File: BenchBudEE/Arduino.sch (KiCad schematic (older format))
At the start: 14 parts

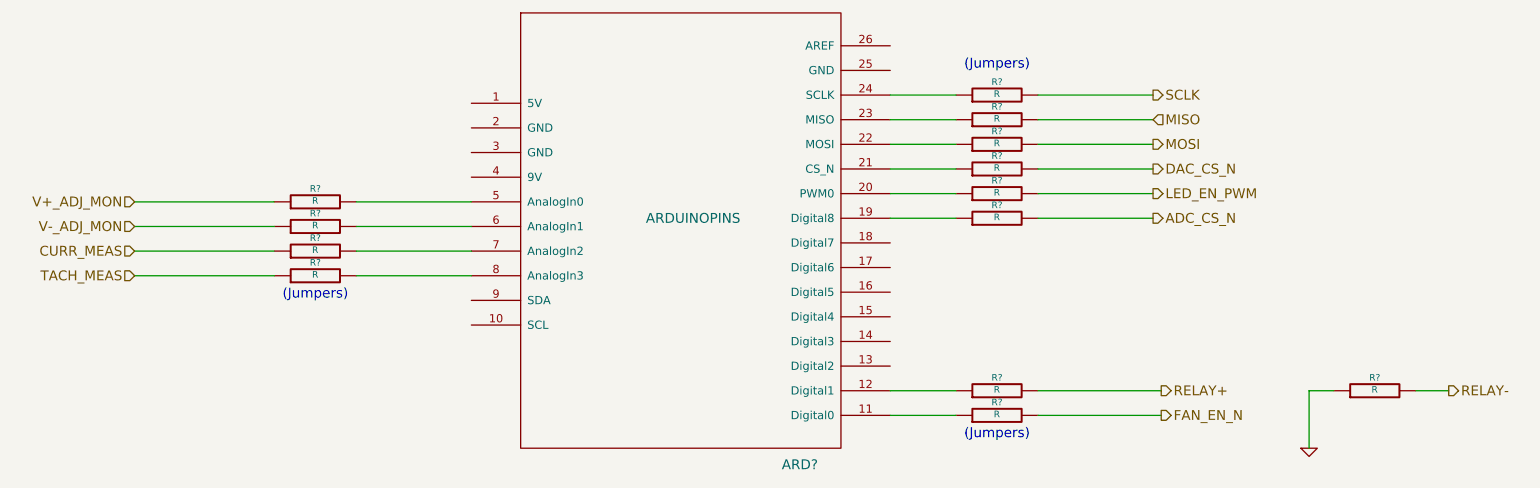
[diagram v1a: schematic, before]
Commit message: Current/fan module refactoring.
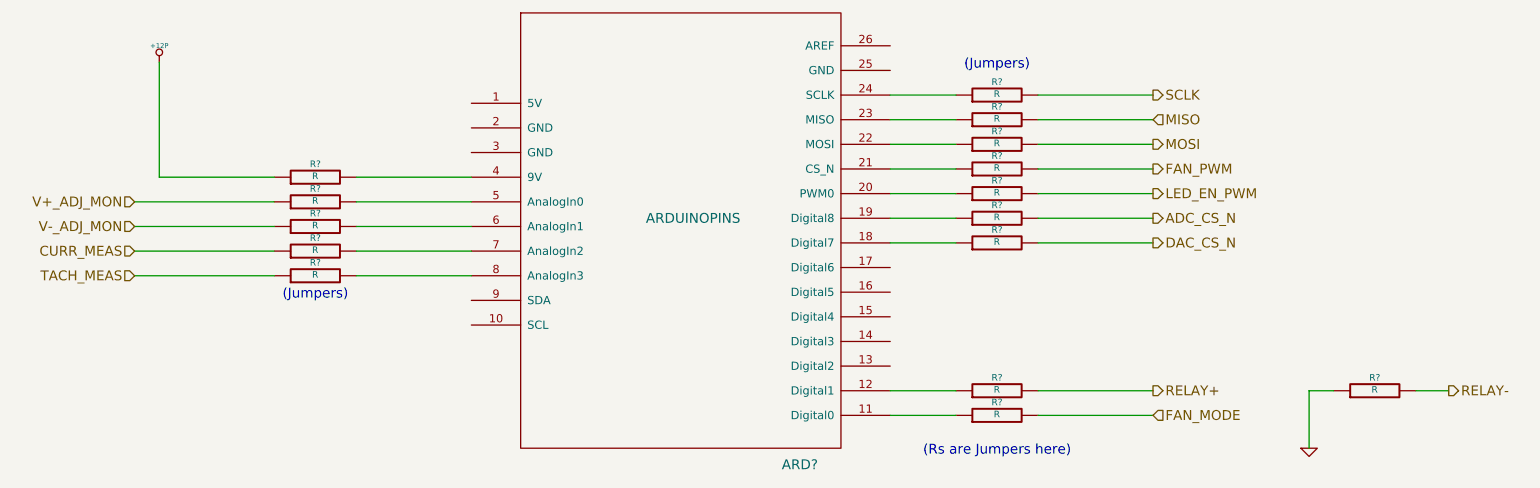
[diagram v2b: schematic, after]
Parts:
- added R? (x2): R, ~, symbol R
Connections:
- net at ARD?.11 (Digital0): now also R?.1; no longer R?.1
- net at ARD?.18 (Digital7): now also R?.1
- net at ARD?.21 (CS_N): now also R?.1; no longer R?.1
- net at ARD?.4 (9V): now also R?.2
- net FAN_EN_N renamed FAN_PWM
- new net +12P: R?.1
- new net FAN_MODE: R?.2
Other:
- note added: "(Rs are Jumpers here)"
- moved on the sheet: R?
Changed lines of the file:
@@
 Comment4 ""
 $EndDescr
-Text HLabel 8700 4750 2    60   Output ~ 0
+Text HLabel 8650 4750 2    60   Output ~ 0
 RELAY+
 Text HLabel 10450 4750 2    60   Output ~ 0
@@
 Text HLabel 8650 2950 2    60   Output ~ 0
 SCLK
+Text HLabel 8650 3850 2    60   Output ~ 0
+DAC_CS_N
 Text HLabel 8650 3400 2    60   Output ~ 0
-DAC_CS_N
-Text HLabel 8700 4900 2    60   Output ~ 0
-FAN_EN_N
+FAN_PWM
 Text HLabel 2450 4050 0    60   Input ~ 0
 TACH_MEAS
@@
 L R R?
 U 1 1 52F90820
-P 7700 4900
-F 0 "R?" V 7780 4900 40  0000 C CNN
-F 1 "R" V 7707 4901 40  0000 C CNN
-F 2 "~" V 7630 4900 30  0000 C CNN
-F 3 "~" H 7700 4900 30  0000 C CNN
-	1    7700 4900
-	0    -1   -1   0
-$EndComp
-Wire Wire Line
-	7450 4900 7050 4900
-Text Notes 7500 5050 0    60   ~ 0
-(Jumpers)
+P 7700 3400
+F 0 "R?" V 7780 3400 40  0000 C CNN
+F 1 "R" V 7707 3401 40  0000 C CNN
+F 2 "~" V 7630 3400 30  0000 C CNN
+F 3 "~" H 7700 3400 30  0000 C CNN
+	1    7700 3400
+	0    -1   -1   0
+$EndComp
+Wire Wire Line
+	7450 3400 7050 3400
+Text Notes 7250 5150 0    60   ~ 0
+(Rs are Jumpers here)
 $Comp
 L R R?
@@
 (Jumpers)
 Wire Wire Line
-	7950 4750 8700 4750
-Wire Wire Line
-	7950 4900 8700 4900
+	7950 4750 8650 4750
+Wire Wire Line
+	7950 3400 8650 3400
 $Comp
 L R R?
 U 1 1 52F92315
-P 7700 3400
-F 0 "R?" V 7780 3400 40  0000 C CNN
-F 1 "R" V 7707 3401 40  0000 C CNN
-F 2 "~" V 7630 3400 30  0000 C CNN
-F 3 "~" H 7700 3400 30  0000 C CNN
-	1    7700 3400
+P 7700 3850
+F 0 "R?" V 7780 3850 40  0000 C CNN
+F 1 "R" V 7707 3851 40  0000 C CNN
+F 2 "~" V 7630 3850 30  0000 C CNN
+F 3 "~" H 7700 3850 30  0000 C CNN
+	1    7700 3850
 	0    -1   -1   0
 $EndComp
@@
 	7450 3250 7050 3250
 Wire Wire Line
-	7050 3400 7450 3400
-Wire Wire Line
-	7950 3400 8650 3400
+	7050 3850 7450 3850
+Wire Wire Line
+	7950 3850 8650 3850
 Wire Wire Line
 	7950 3250 8650 3250
@@
 Wire Wire Line
 	7950 3700 8650 3700
+Text HLabel 8650 4900 2    60   Input ~ 0
+FAN_MODE
+$Comp
+L R R?
+U 1 1 52FAF6A4
+P 7700 4900
+F 0 "R?" V 7780 4900 40  0000 C CNN
+F 1 "R" V 7707 4901 40  0000 C CNN
+F 2 "~" V 7630 4900 30  0000 C CNN
+F 3 "~" H 7700 4900 30  0000 C CNN
+	1    7700 4900
+	0    -1   -1   0
+$EndComp
+Wire Wire Line
+	7950 4900 8650 4900
+Wire Wire Line
+	7450 4900 7050 4900
+$Comp
+L R R?
+U 1 1 52FAFDE4
+P 3550 3450
+F 0 "R?" V 3630 3450 40  0000 C CNN
+F 1 "R" V 3557 3451 40  0000 C CNN
+F 2 "~" V 3480 3450 30  0000 C CNN
+F 3 "~" H 3550 3450 30  0000 C CNN
+	1    3550 3450
+	0    -1   -1   0
+$EndComp
+Wire Wire Line
+	3800 3450 4500 3450
+Wire Wire Line
+	3300 3450 2600 3450
+Wire Wire Line
+	2600 3450 2600 2750
+$Comp
+L +12P #PWR?
+U 1 1 52FAFE2B
+P 2600 2750
+F 0 "#PWR?" H 2600 2720 30  0001 C CNN
+F 1 "+12P" H 2600 2850 30  0000 C CNN
+F 2 "" H 2600 2750 60  0000 C CNN
+F 3 "" H 2600 2750 60  0000 C CNN
+	1    2600 2750
+	1    0    0    -1
+$EndComp
 $EndSCHEMATC

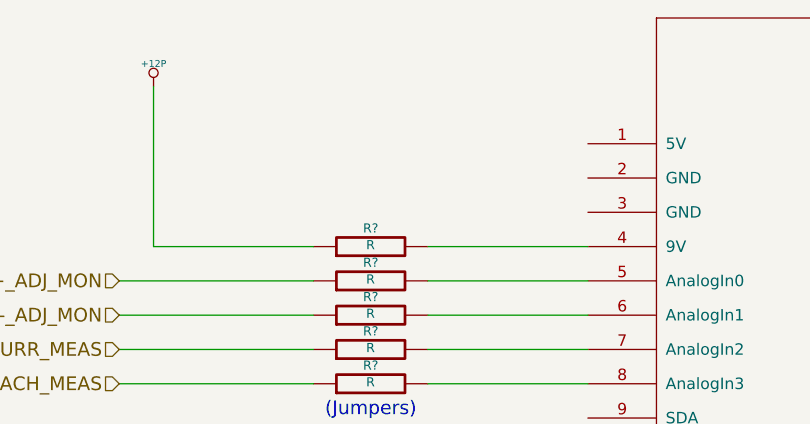
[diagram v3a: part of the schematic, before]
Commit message: Connected Arduino power/ground. +5V power filtering. Removed current monitoring.
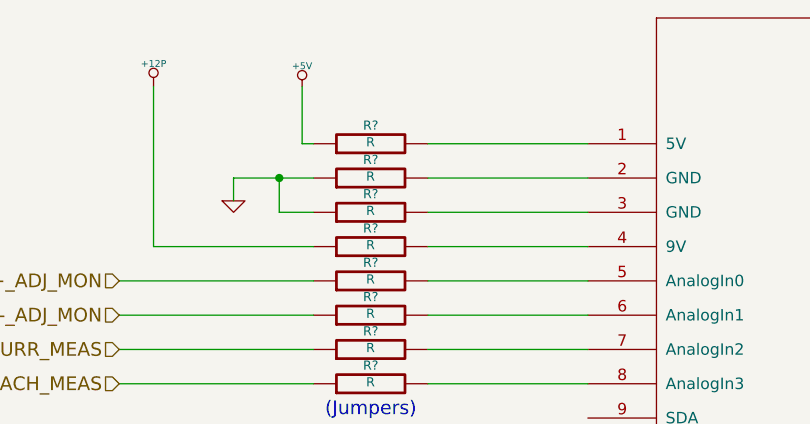
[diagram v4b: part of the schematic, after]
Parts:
- added R? (x3): R, ~, symbol R
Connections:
- net GND: now also R?.1, R?.1
- net at ARD?.1 (5V): now also R?.2
- net at ARD?.2 (GND): now also R?.2
- net at ARD?.3 (GND): now also R?.2
- new net +5V: R?.1
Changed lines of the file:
@@
 Sheet 9 9
 Title ""
-Date "14 feb 2014"
+Date "19 feb 2014"
 Rev ""
 Comp ""
@@
 	1    0    0    -1
 $EndComp
+$Comp
+L R R?
+U 1 1 53043434
+P 3550 3000
+F 0 "R?" V 3630 3000 40  0000 C CNN
+F 1 "R" V 3557 3001 40  0000 C CNN
+F 2 "~" V 3480 3000 30  0000 C CNN
+F 3 "~" H 3550 3000 30  0000 C CNN
+	1    3550 3000
+	0    -1   -1   0
+$EndComp
+Wire Wire Line
+	3800 3000 4500 3000
+Wire Wire Line
+	3300 3000 3250 3000
+Wire Wire Line
+	3250 3000 3250 2750
+$Comp
+L +5V #PWR?
+U 1 1 53043481
+P 3250 2750
+F 0 "#PWR?" H 3250 2840 20  0001 C CNN
+F 1 "+5V" H 3250 2840 30  0000 C CNN
+F 2 "" H 3250 2750 60  0000 C CNN
+F 3 "" H 3250 2750 60  0000 C CNN
+	1    3250 2750
+	1    0    0    -1
+$EndComp
+$Comp
+L R R?
+U 1 1 5304348E
+P 3550 3150
+F 0 "R?" V 3630 3150 40  0000 C CNN
+F 1 "R" V 3557 3151 40  0000 C CNN
+F 2 "~" V 3480 3150 30  0000 C CNN
+F 3 "~" H 3550 3150 30  0000 C CNN
+	1    3550 3150
+	0    -1   -1   0
+$EndComp
+$Comp
+L R R?
+U 1 1 53043494
+P 3550 3300
+F 0 "R?" V 3630 3300 40  0000 C CNN
+F 1 "R" V 3557 3301 40  0000 C CNN
+F 2 "~" V 3480 3300 30  0000 C CNN
+F 3 "~" H 3550 3300 30  0000 C CNN
+	1    3550 3300
+	0    -1   -1   0
+$EndComp
+Wire Wire Line
+	4500 3150 3800 3150
+Wire Wire Line
+	3300 3150 2950 3150
+Wire Wire Line
+	2950 3150 2950 3250
+$Comp
+L GND #PWR?
+U 1 1 5304350C
+P 2950 3250
+F 0 "#PWR?" H 2950 3250 30  0001 C CNN
+F 1 "GND" H 2950 3180 30  0001 C CNN
+F 2 "" H 2950 3250 60  0000 C CNN
+F 3 "" H 2950 3250 60  0000 C CNN
+	1    2950 3250
+	1    0    0    -1
+$EndComp
+Wire Wire Line
+	3300 3300 3150 3300
+Wire Wire Line
+	3150 3300 3150 3150
+Connection ~ 3150 3150
+Wire Wire Line
+	3800 3300 4500 3300
 $EndSCHEMATC

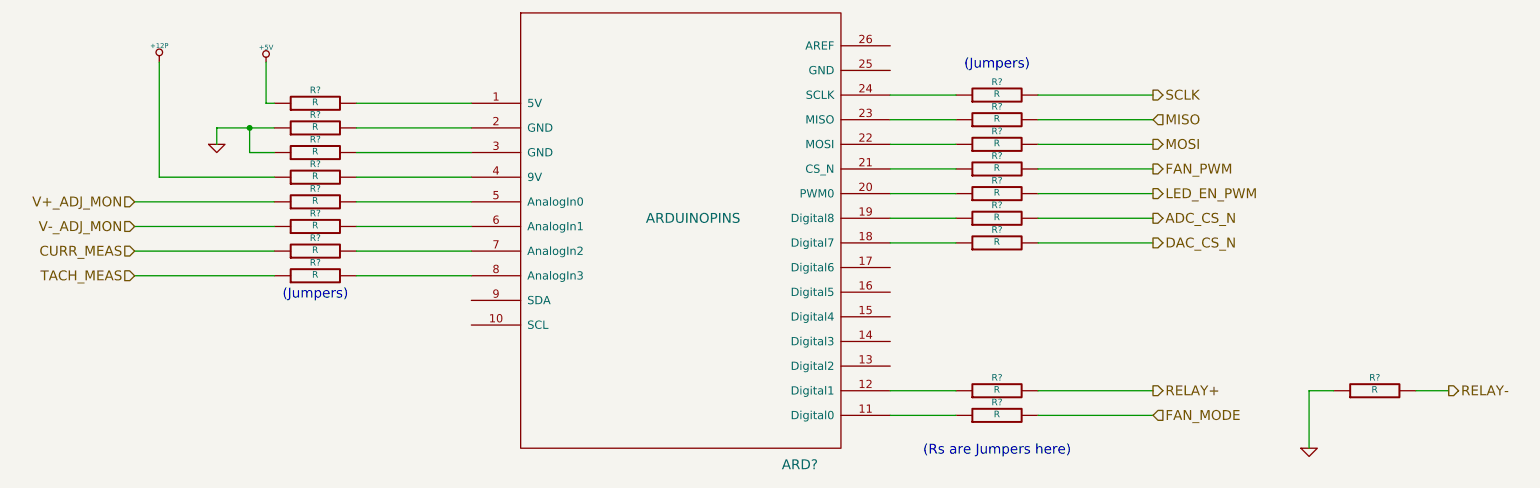
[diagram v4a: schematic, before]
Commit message: Placed the relay components.
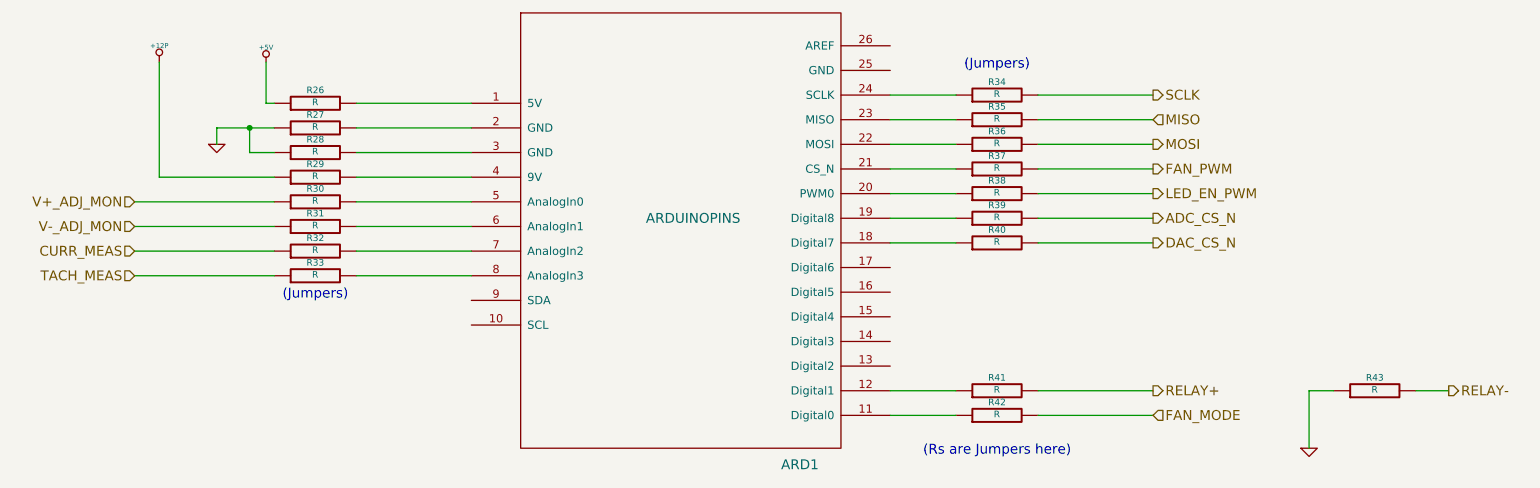
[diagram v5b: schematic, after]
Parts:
- gave numbers to parts that had none: 19
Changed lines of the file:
@@
 Sheet 9 9
 Title ""
-Date "19 feb 2014"
+Date "20 feb 2014"
 Rev ""
 Comp ""
@@
 TACH_MEAS
 $Comp
-L ARDUINOPINS ARD?
+L ARDUINOPINS ARD1
 U 1 1 52F9043E
 P 5800 3700
-F 0 "ARD?" H 6500 2200 60  0000 C CNN
+F 0 "ARD1" H 6500 2200 60  0000 C CNN
 F 1 "ARDUINOPINS" H 5850 3700 60  0000 C CNN
 F 2 "" H 5850 3200 60  0000 C CNN
@@
 CURR_MEAS
 $Comp
-L R R?
+L R R37
 U 1 1 52F90820
 P 7700 3400
-F 0 "R?" V 7780 3400 40  0000 C CNN
+F 0 "R37" V 7780 3400 40  0000 C CNN
 F 1 "R" V 7707 3401 40  0000 C CNN
 F 2 "~" V 7630 3400 30  0000 C CNN
@@
 (Rs are Jumpers here)
 $Comp
-L R R?
+L R R41
 U 1 1 52F90A97
 P 7700 4750
-F 0 "R?" V 7780 4750 40  0000 C CNN
+F 0 "R41" V 7780 4750 40  0000 C CNN
 F 1 "R" V 7707 4751 40  0000 C CNN
 F 2 "~" V 7630 4750 30  0000 C CNN
@@
 	7050 4750 7450 4750
 $Comp
-L GND #PWR?
+L GND #PWR55
 U 1 1 52F915E6
 P 9600 5100
-F 0 "#PWR?" H 9600 5100 30  0001 C CNN
+F 0 "#PWR55" H 9600 5100 30  0001 C CNN
 F 1 "GND" H 9600 5030 30  0001 C CNN
 F 2 "" H 9600 5100 60  0000 C CNN
@@
 $EndComp
 $Comp
-L R R?
+L R R33
 U 1 1 52F9185A
 P 3550 4050
-F 0 "R?" V 3630 4050 40  0000 C CNN
+F 0 "R33" V 3630 4050 40  0000 C CNN
 F 1 "R" V 3557 4051 40  0000 C CNN
 F 2 "~" V 3480 4050 30  0000 C CNN
@@
 $EndComp
 $Comp
-L R R?
+L R R32
 U 1 1 52F91860
 P 3550 3900
-F 0 "R?" V 3630 3900 40  0000 C CNN
+F 0 "R32" V 3630 3900 40  0000 C CNN
 F 1 "R" V 3557 3901 40  0000 C CNN
 F 2 "~" V 3480 3900 30  0000 C CNN
@@
 V-_ADJ_MON
 $Comp
-L R R?
+L R R31
 U 1 1 52F91E08
 P 3550 3750
-F 0 "R?" V 3630 3750 40  0000 C CNN
+F 0 "R31" V 3630 3750 40  0000 C CNN
 F 1 "R" V 3557 3751 40  0000 C CNN
 F 2 "~" V 3480 3750 30  0000 C CNN
@@
 $EndComp
 $Comp
-L R R?
+L R R30
 U 1 1 52F91E0E
 P 3550 3600
-F 0 "R?" V 3630 3600 40  0000 C CNN
+F 0 "R30" V 3630 3600 40  0000 C CNN
 F 1 "R" V 3557 3601 40  0000 C CNN
 F 2 "~" V 3480 3600 30  0000 C CNN
@@
 	7950 3400 8650 3400
 $Comp
-L R R?
+L R R40
 U 1 1 52F92315
 P 7700 3850
-F 0 "R?" V 7780 3850 40  0000 C CNN
+F 0 "R40" V 7780 3850 40  0000 C CNN
 F 1 "R" V 7707 3851 40  0000 C CNN
 F 2 "~" V 7630 3850 30  0000 C CNN
@@
 $EndComp
 $Comp
-L R R?
+L R R36
 U 1 1 52F9231B
 P 7700 3250
-F 0 "R?" V 7780 3250 40  0000 C CNN
+F 0 "R36" V 7780 3250 40  0000 C CNN
 F 1 "R" V 7707 3251 40  0000 C CNN
 F 2 "~" V 7630 3250 30  0000 C CNN
@@
 $EndComp
 $Comp
-L R R?
+L R R35
 U 1 1 52F92321
 P 7700 3100
-F 0 "R?" V 7780 3100 40  0000 C CNN
+F 0 "R35" V 7780 3100 40  0000 C CNN
 F 1 "R" V 7707 3101 40  0000 C CNN
 F 2 "~" V 7630 3100 30  0000 C CNN
@@
 $EndComp
 $Comp
-L R R?
+L R R34
 U 1 1 52F92327
 P 7700 2950
-F 0 "R?" V 7780 2950 40  0000 C CNN
+F 0 "R34" V 7780 2950 40  0000 C CNN
 F 1 "R" V 7707 2951 40  0000 C CNN
 F 2 "~" V 7630 2950 30  0000 C CNN
@@
 (Jumpers)
 $Comp
-L R R?
+L R R43
 U 1 1 52F923CE
 P 10000 4750
-F 0 "R?" V 10080 4750 40  0000 C CNN
+F 0 "R43" V 10080 4750 40  0000 C CNN
 F 1 "R" V 10007 4751 40  0000 C CNN
 F 2 "~" V 9930 4750 30  0000 C CNN
@@
 LED_EN_PWM
 $Comp
-L R R?
+L R R38
 U 1 1 52F92652
 P 7700 3550
-F 0 "R?" V 7780 3550 40  0000 C CNN
+F 0 "R38" V 7780 3550 40  0000 C CNN
 F 1 "R" V 7707 3551 40  0000 C CNN
 F 2 "~" V 7630 3550 30  0000 C CNN
@@
 ADC_CS_N
 $Comp
-L R R?
+L R R39
 U 1 1 52F9D11D
 P 7700 3700
-F 0 "R?" V 7780 3700 40  0000 C CNN
+F 0 "R39" V 7780 3700 40  0000 C CNN
 F 1 "R" V 7707 3701 40  0000 C CNN
 F 2 "~" V 7630 3700 30  0000 C CNN
@@
 FAN_MODE
 $Comp
-L R R?
+L R R42
 U 1 1 52FAF6A4
 P 7700 4900
-F 0 "R?" V 7780 4900 40  0000 C CNN
+F 0 "R42" V 7780 4900 40  0000 C CNN
 F 1 "R" V 7707 4901 40  0000 C CNN
 F 2 "~" V 7630 4900 30  0000 C CNN
@@
 	7450 4900 7050 4900
 $Comp
-L R R?
+L R R29
 U 1 1 52FAFDE4
 P 3550 3450
-F 0 "R?" V 3630 3450 40  0000 C CNN
+F 0 "R29" V 3630 3450 40  0000 C CNN
 F 1 "R" V 3557 3451 40  0000 C CNN
 F 2 "~" V 3480 3450 30  0000 C CNN
@@
 	2600 3450 2600 2750
 $Comp
-L +12P #PWR?
+L +12P #PWR52
 U 1 1 52FAFE2B
 P 2600 2750
-F 0 "#PWR?" H 2600 2720 30  0001 C CNN
+F 0 "#PWR52" H 2600 2720 30  0001 C CNN
 F 1 "+12P" H 2600 2850 30  0000 C CNN
 F 2 "" H 2600 2750 60  0000 C CNN
@@
 $EndComp
 $Comp
-L R R?
+L R R26
 U 1 1 53043434
 P 3550 3000
-F 0 "R?" V 3630 3000 40  0000 C CNN
+F 0 "R26" V 3630 3000 40  0000 C CNN
 F 1 "R" V 3557 3001 40  0000 C CNN
 F 2 "~" V 3480 3000 30  0000 C CNN
@@
 	3250 3000 3250 2750
 $Comp
-L +5V #PWR?
+L +5V #PWR54
 U 1 1 53043481
 P 3250 2750
-F 0 "#PWR?" H 3250 2840 20  0001 C CNN
+F 0 "#PWR54" H 3250 2840 20  0001 C CNN
 F 1 "+5V" H 3250 2840 30  0000 C CNN
 F 2 "" H 3250 2750 60  0000 C CNN
@@
 $EndComp
 $Comp
-L R R?
+L R R27
 U 1 1 5304348E
 P 3550 3150
-F 0 "R?" V 3630 3150 40  0000 C CNN
+F 0 "R27" V 3630 3150 40  0000 C CNN
 F 1 "R" V 3557 3151 40  0000 C CNN
 F 2 "~" V 3480 3150 30  0000 C CNN
@@
 $EndComp
 $Comp
-L R R?
+L R R28
 U 1 1 53043494
 P 3550 3300
-F 0 "R?" V 3630 3300 40  0000 C CNN
+F 0 "R28" V 3630 3300 40  0000 C CNN
 F 1 "R" V 3557 3301 40  0000 C CNN
 F 2 "~" V 3480 3300 30  0000 C CNN
@@
 	2950 3150 2950 3250
 $Comp
-L GND #PWR?
+L GND #PWR53
 U 1 1 5304350C
 P 2950 3250
-F 0 "#PWR?" H 2950 3250 30  0001 C CNN
+F 0 "#PWR53" H 2950 3250 30  0001 C CNN
 F 1 "GND" H 2950 3180 30  0001 C CNN
 F 2 "" H 2950 3250 60  0000 C CNN

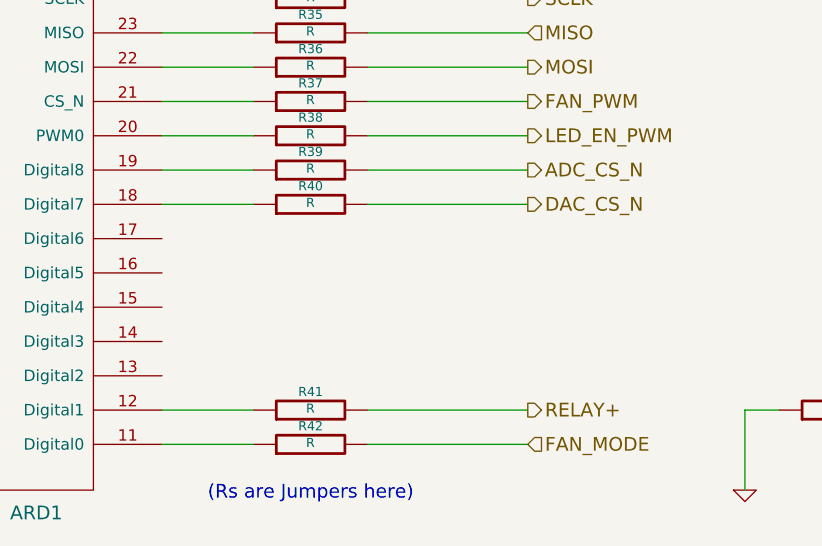
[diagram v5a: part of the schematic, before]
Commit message: Associated the Thermocouple components.
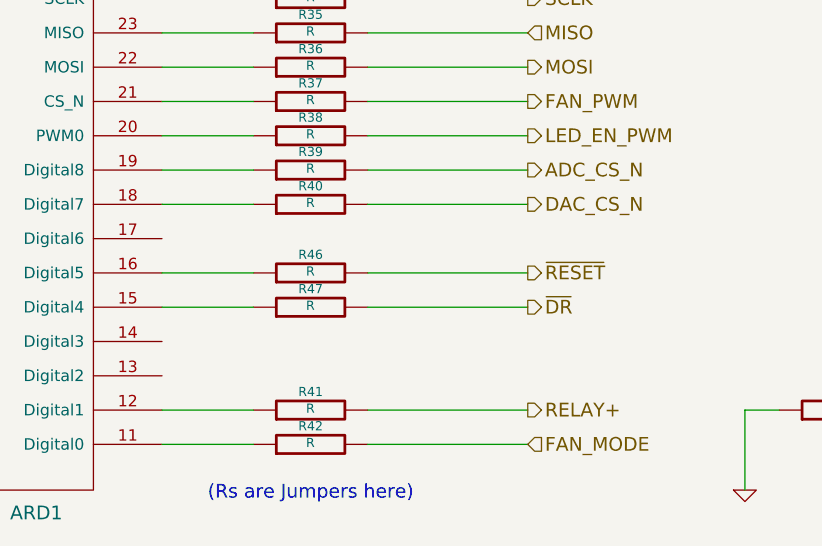
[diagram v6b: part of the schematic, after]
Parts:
- added R46, R47: R, ~, symbol R
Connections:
- net at ARD1.15 (Digital4): now also R47.1
- net at ARD1.16 (Digital5): now also R46.1
- new net ~DR: R47.2
- new net ~RESET: R46.2
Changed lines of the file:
@@
 Sheet 9 9
 Title ""
-Date "20 feb 2014"
+Date "21 feb 2014"
 Rev ""
 Comp ""
@@
 	7050 4750 7450 4750
 $Comp
-L GND #PWR55
+L GND #PWR056
 U 1 1 52F915E6
 P 9600 5100
-F 0 "#PWR55" H 9600 5100 30  0001 C CNN
+F 0 "#PWR056" H 9600 5100 30  0001 C CNN
 F 1 "GND" H 9600 5030 30  0001 C CNN
 F 2 "" H 9600 5100 60  0000 C CNN
@@
 	2600 3450 2600 2750
 $Comp
-L +12P #PWR52
+L +12P #PWR057
 U 1 1 52FAFE2B
 P 2600 2750
-F 0 "#PWR52" H 2600 2720 30  0001 C CNN
+F 0 "#PWR057" H 2600 2720 30  0001 C CNN
 F 1 "+12P" H 2600 2850 30  0000 C CNN
 F 2 "" H 2600 2750 60  0000 C CNN
@@
 	3250 3000 3250 2750
 $Comp
-L +5V #PWR54
+L +5V #PWR058
 U 1 1 53043481
 P 3250 2750
-F 0 "#PWR54" H 3250 2840 20  0001 C CNN
+F 0 "#PWR058" H 3250 2840 20  0001 C CNN
 F 1 "+5V" H 3250 2840 30  0000 C CNN
 F 2 "" H 3250 2750 60  0000 C CNN
@@
 	2950 3150 2950 3250
 $Comp
-L GND #PWR53
+L GND #PWR059
 U 1 1 5304350C
 P 2950 3250
-F 0 "#PWR53" H 2950 3250 30  0001 C CNN
+F 0 "#PWR059" H 2950 3250 30  0001 C CNN
 F 1 "GND" H 2950 3180 30  0001 C CNN
 F 2 "" H 2950 3250 60  0000 C CNN
@@
 Wire Wire Line
 	3800 3300 4500 3300
+Text HLabel 8650 4150 2    60   Output ~ 0
+~RESET
+$Comp
+L R R46
+U 1 1 5307465F
+P 7700 4150
+F 0 "R46" V 7780 4150 40  0000 C CNN
+F 1 "R" V 7707 4151 40  0000 C CNN
+F 2 "~" V 7630 4150 30  0000 C CNN
+F 3 "~" H 7700 4150 30  0000 C CNN
+	1    7700 4150
+	0    -1   -1   0
+$EndComp
+Wire Wire Line
+	7050 4150 7450 4150
+Wire Wire Line
+	7950 4150 8650 4150
+Text HLabel 8650 4300 2    60   Output ~ 0
+~DR
+$Comp
+L R R47
+U 1 1 53074668
+P 7700 4300
+F 0 "R47" V 7780 4300 40  0000 C CNN
+F 1 "R" V 7707 4301 40  0000 C CNN
+F 2 "~" V 7630 4300 30  0000 C CNN
+F 3 "~" H 7700 4300 30  0000 C CNN
+	1    7700 4300
+	0    -1   -1   0
+$EndComp
+Wire Wire Line
+	7050 4300 7450 4300
+Wire Wire Line
+	7950 4300 8650 4300
 $EndSCHEMATC
